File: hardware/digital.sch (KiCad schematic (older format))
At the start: 39 parts, among them U10 74LVC4245, U11 74LVC4245, U12 74LVC4245, U9 STM32F103V8Tx

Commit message: Schematic mainly done. Working on PCB layout in isolated blocks.
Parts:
- removed C49, C50, C51, C52, C53, C54, C55, C56, C57: 100n, Capacitor_SMD:C_0603_1608Metric, symbol Device:C
- removed U10, U11, U12: 74LVC4245, Package_SO:TSSOP-24_4.4x7.8mm_P0.65mm, symbol Logic_LevelTranslator:SN74AVC8T245PW
- added C17: 1u0, Capacitor_SMD:C_0603_1608Metric, symbol Device:C_Small
- added C18, C19: C_Small, Capacitor_SMD:C_0603_1608Metric, symbol Device:C_Small
- added C20: 10n, Capacitor_SMD:C_0603_1608Metric, symbol Device:C_Small
- added C28, C29, C30, C31, C32, C33, C34, C35, C36: 100n, Capacitor_SMD:C_0603_1608Metric, symbol Device:C
- added J10: Conn_02x03_Counter_Clockwise, Connector_PinSocket_2.54mm:PinSocket_2x03_P2.54mm_Vertical_SMD, symbol Connector_Generic:Conn_02x03_Counter_Clockwise
- added J11: Conn_02x05_Odd_Even, Connector_PinHeader_1.27mm:PinHeader_2x05_P1.27mm_Vertical_SMD, symbol Connector_Generic:Conn_02x05_Odd_Even
- added R10, R11, R9: 10K, Resistor_SMD:R_0603_1608Metric, symbol Device:R_Small
- added RN18, RN19, RN20, RN21, RN22, RN23: 4K7, Resistor_SMD:R_Array_Convex_4x0603, symbol Device:R_Pack04
- added SW1: SW_Push, symbol Switch:SW_Push
- added U10, U11, U9: 74LVC4245, Package_SO:TSSOP-24_4.4x7.8mm_P0.65mm, symbol Console2JAMMA:74LVC4245
- added Y1: 8MHz, Crystal:Crystal_SMD_5032-2Pin_5.0x3.2mm, symbol Device:Crystal_Small
- C16: renamed from C41; footprint Capacitor_SMD:C_0603_1608Metric -> Capacitor_SMD:C_0805_2012Metric
- C27: renamed from C48; footprint Capacitor_SMD:C_0603_1608Metric -> Capacitor_SMD:C_0805_2012Metric
- renumbered C42 to C21, C43 to C22, C44 to C23, C45 to C24, C46 to C25, C47 to C26, R14 to R12, R15 to R13, R16 to R14, U9 to U8
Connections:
- net labels added: Audio_Select_L, Audio_Select_Mono, Audio_Select_R, BOOT0, BOOT1, TCK_SWCLK, TDI_NC, TDO_TRACESWO, TMS_SWDIO, USB_D+, USB_D-, VOL_CLK, VOL_DATA_IN, VOL_LOAD_SHIFT, Video_Select_Blue, Video_Select_CSYNC, Video_Select_Green, Video_Select_Red, ~TRST~
- net labels removed: P1P2_Shifter_DIR
- wire segments 304 -> 453
- no-connect marks 1 -> 12
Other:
- note added: "Boot Loader Config"
- note added: "Cortex Debug Header"
- note added: "KEY"
- note added: "Non 5V tolerant I/O: PC0-5, PA1-7, PB0-1, 5"
- note removed: "3V3 I/O to and from Level Shifter"
- note removed: "Player 1"
- note removed: "Player 2"
- moved on the sheet: C16, C21, C22, C23, C24, C25, C26, C27, R12, R13, R14, RN10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

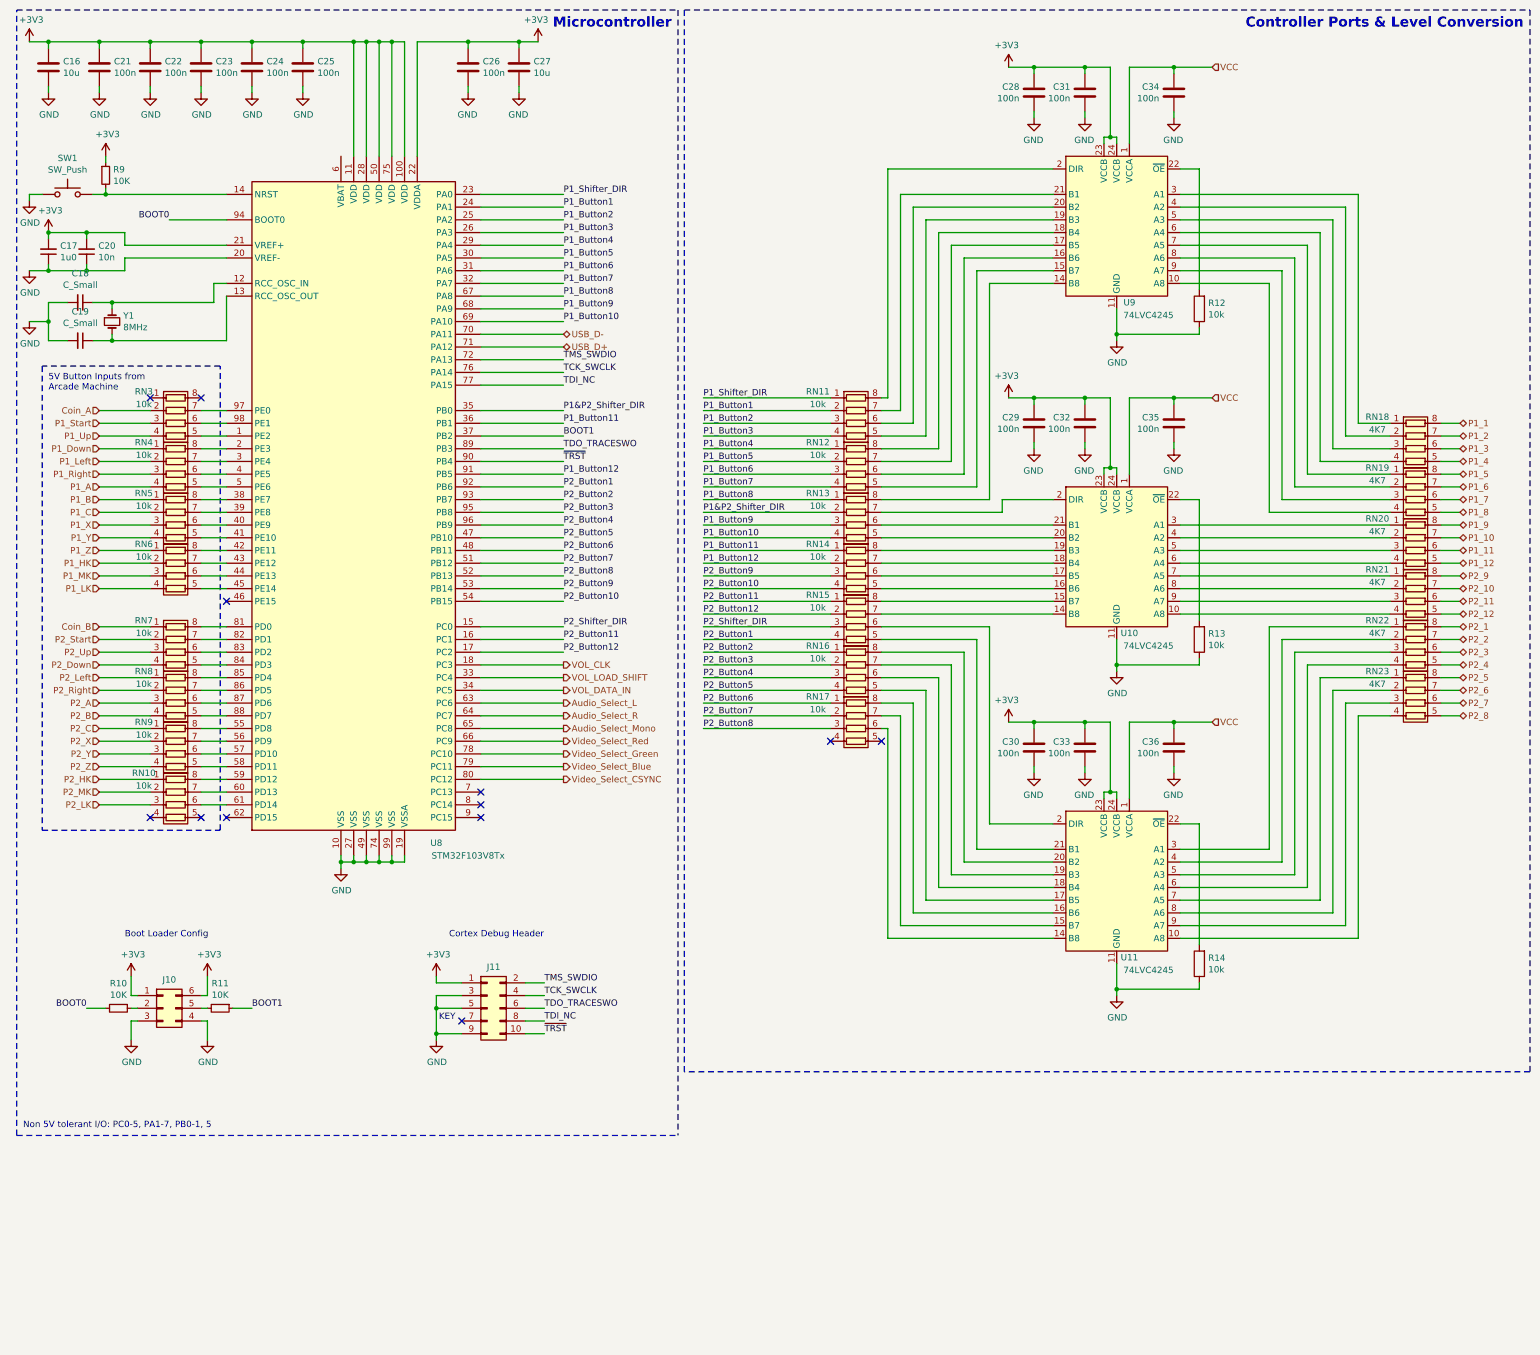
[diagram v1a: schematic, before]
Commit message: Completing the functionality of PCB layout. Require silkscreen placement still, though.
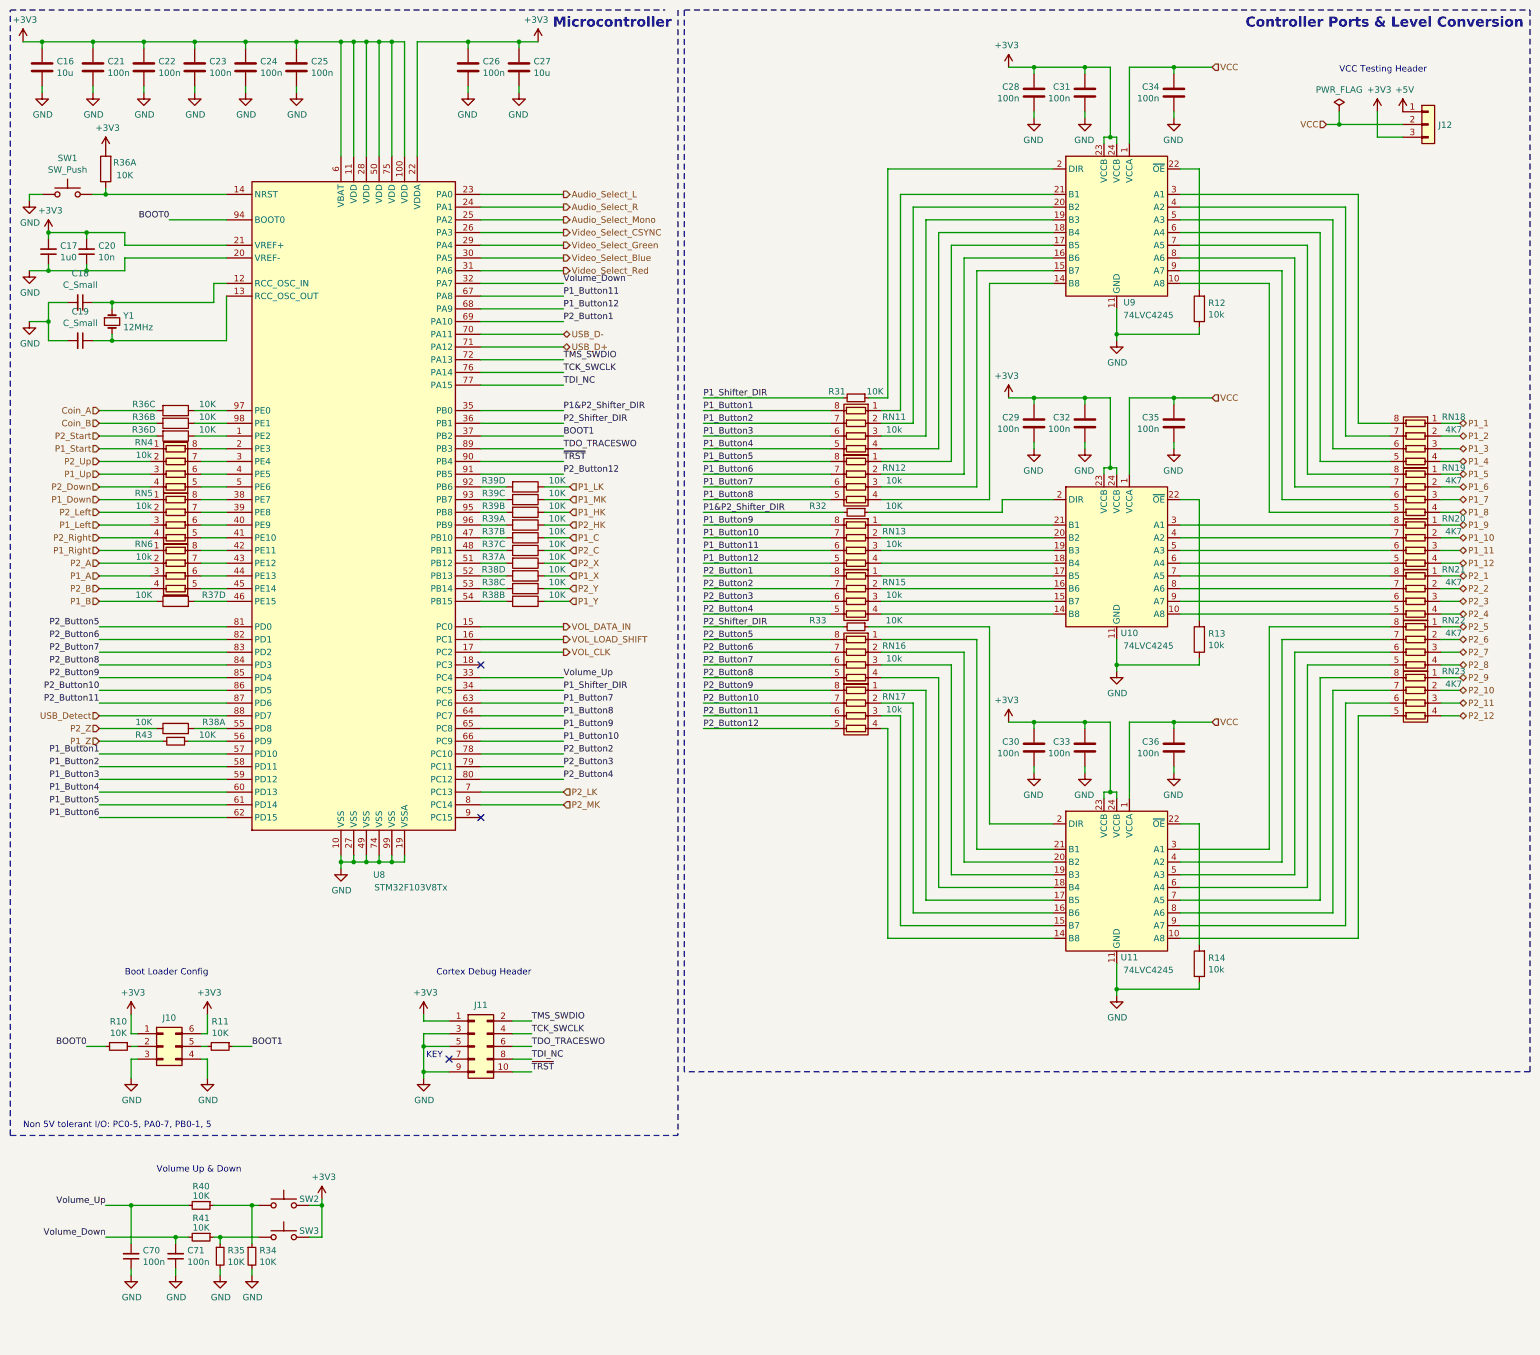
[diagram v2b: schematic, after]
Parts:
- removed R9: 10K, Resistor_SMD:R_0603_1608Metric, symbol Device:R_Small
- removed RN10, RN14, RN3, RN7, RN8, RN9: 10k, Resistor_SMD:R_Array_Convex_4x0603, symbol Device:R_Pack04
- added C70, C71: 100n, Capacitor_SMD:C_0603_1608Metric, symbol Device:C_Small
- added J12: Conn_01x03, Connector_PinHeader_2.54mm:PinHeader_1x03_P2.54mm_Vertical, symbol Connector_Generic:Conn_01x03
- added R31, R32, R33, R34, R35, R40, R41, R43: 10K, Resistor_SMD:R_0603_1608Metric, symbol Device:R_Small
- added R36, R37, R38, R39: 10K, Resistor_SMD:R_Array_Convex_4x0603, symbol Device:R_Pack04_Split
- added SW2, SW3: SW_Push, Console2JAMMA:SW_Push_SPST_NO_Alps_SKRP, symbol Switch:SW_Push
- SW1: footprint (none) -> Console2JAMMA:SW_Push_SPST_NO_Alps_SKRP
- Y1: value 8MHz -> 12MHz
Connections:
- net +3V3: now also U8.6 (VBAT), J12.3 (Pin_3), R36.1, SW2.2, SW3.2
- net Audio_Select_L: now also U8.23 (PA0); no longer U8.63 (PC6)
- net Audio_Select_Mono: now also U8.25 (PA2); no longer U8.65 (PC8)
- net Audio_Select_R: now also U8.24 (PA1); no longer U8.64 (PC7)
- net Coin_A: now also R36.3
- net Coin_B: now also R36.2
- net GND: now also C70.1, C71.1, R34.2, R35.2
- net P1&P2_Shifter_DIR: now also R32.2; no longer RN13.2 (R2.1)
- net P1_1: now also RN18.1 (R1.1); no longer RN18.8 (R1.2)
- net P1_10: now also RN20.2 (R2.1); no longer RN20.7 (R2.2)
- net P1_11: now also RN20.3 (R3.1); no longer RN20.6 (R3.2)
- net P1_12: now also RN20.4 (R4.1); no longer RN20.5 (R4.2)
- net P1_2: now also RN18.2 (R2.1); no longer RN18.7 (R2.2)
- net P1_3: now also RN18.3 (R3.1); no longer RN18.6 (R3.2)
- net P1_4: now also RN18.4 (R4.1); no longer RN18.5 (R4.2)
- net P1_5: now also RN19.1 (R1.1); no longer RN19.8 (R1.2)
- net P1_6: now also RN19.2 (R2.1); no longer RN19.7 (R2.2)
- net P1_7: now also RN19.3 (R3.1); no longer RN19.6 (R3.2)
- net P1_8: now also RN19.4 (R4.1); no longer RN19.5 (R4.2)
- net P1_9: now also RN20.1 (R1.1); no longer RN20.8 (R1.2)
- net P1_A: now also RN6.3 (R3.1); no longer RN4.4 (R4.1)
- net P1_B: now also R37.5; no longer RN5.1 (R1.1)
- net P1_Button1: now also RN11.8 (R1.2), U8.57 (PD10); no longer RN11.2 (R2.1), U8.24 (PA1)
- net P1_Button10: now also RN13.7 (R2.2), U8.66 (PC9); no longer RN13.4 (R4.1), U8.69 (PA10)
- net P1_Button11: now also RN13.6 (R3.2), U8.67 (PA8); no longer U8.36 (PB1)
- net P1_Button12: now also RN13.5 (R4.2), U8.68 (PA9); no longer U8.91 (PB5)
- net P1_Button2: now also RN11.7 (R2.2), U8.58 (PD11); no longer RN11.3 (R3.1), U8.25 (PA2)
- net P1_Button3: now also RN11.6 (R3.2), U8.59 (PD12); no longer RN11.4 (R4.1), U8.26 (PA3)
- net P1_Button4: now also RN11.5 (R4.2), U8.60 (PD13); no longer RN12.1 (R1.1), U8.29 (PA4)
- net P1_Button5: now also RN12.8 (R1.2), U8.61 (PD14); no longer RN12.2 (R2.1), U8.30 (PA5)
- net P1_Button6: now also RN12.7 (R2.2), U8.62 (PD15); no longer RN12.3 (R3.1), U8.31 (PA6)
- net P1_Button7: now also RN12.6 (R3.2), U8.63 (PC6); no longer RN12.4 (R4.1), U8.32 (PA7)
- net P1_Button8: now also RN12.5 (R4.2), U8.64 (PC7); no longer RN13.1 (R1.1), U8.67 (PA8)
- net P1_Button9: now also RN13.8 (R1.2), U8.65 (PC8); no longer RN13.3 (R3.1), U8.68 (PA9)
- net P1_C: now also R37.7; no longer RN5.2 (R2.1)
- net P1_Down: now also RN5.1 (R1.1); no longer RN4.1 (R1.1)
- net P1_HK: now also R39.7; no longer RN6.2 (R2.1)
- net P1_LK: now also R39.5; no longer RN6.4 (R4.1)
- net P1_Left: now also RN5.3 (R3.1); no longer RN4.2 (R2.1)
- net P1_MK: now also R39.6; no longer RN6.3 (R3.1)
- net P1_Right: now also RN6.1 (R1.1); no longer RN4.3 (R3.1)
- net P1_Shifter_DIR: now also U8.34 (PC5), R31.2; no longer RN11.1 (R1.1), U8.23 (PA0)
- net P1_Start: now also RN4.1 (R1.1)
- net P1_Up: now also RN4.3 (R3.1)
- net P1_X: now also R38.5; no longer RN5.3 (R3.1)
- net P1_Y: now also R38.7; no longer RN5.4 (R4.1)
- net P1_Z: now also R43.2; no longer RN6.1 (R1.1)
- net P2_1: now also RN21.1 (R1.1); no longer RN22.8 (R1.2)
- net P2_10: now also RN23.2 (R2.1); no longer RN21.7 (R2.2)
- net P2_11: now also RN23.3 (R3.1); no longer RN21.6 (R3.2)
- net P2_12: now also RN23.4 (R4.1); no longer RN21.5 (R4.2)
- net P2_2: now also RN21.2 (R2.1); no longer RN22.7 (R2.2)
- net P2_3: now also RN21.3 (R3.1); no longer RN22.6 (R3.2)
- net P2_4: now also RN21.4 (R4.1); no longer RN22.5 (R4.2)
- net P2_5: now also RN22.1 (R1.1); no longer RN23.8 (R1.2)
- net P2_6: now also RN22.2 (R2.1); no longer RN23.7 (R2.2)
- net P2_7: now also RN22.3 (R3.1); no longer RN23.6 (R3.2)
- net P2_8: now also RN22.4 (R4.1); no longer RN23.5 (R4.2)
- net P2_9: now also RN23.1 (R1.1); no longer RN21.8 (R1.2)
- net P2_A: now also RN6.2 (R2.1)
- net P2_B: now also RN6.4 (R4.1)
- net P2_Button1: now also RN15.8 (R1.2), U8.69 (PA10); no longer RN15.4 (R4.1), U8.92 (PB6)
- net P2_Button10: now also RN17.7 (R2.2), U8.86 (PD5); no longer U8.54 (PB15)
- net P2_Button11: now also RN17.6 (R3.2), U8.87 (PD6); no longer RN15.1 (R1.1), U8.16 (PC1)
- net P2_Button12: now also RN17.5 (R4.2), U8.91 (PB5); no longer RN15.2 (R2.1), U8.17 (PC2)
- net P2_Button2: now also RN15.7 (R2.2), U8.78 (PC10); no longer RN16.1 (R1.1), U8.93 (PB7)
- net P2_Button3: now also RN15.6 (R3.2), U8.79 (PC11); no longer RN16.2 (R2.1), U8.95 (PB8)
- net P2_Button4: now also RN15.5 (R4.2), U8.80 (PC12); no longer RN16.3 (R3.1), U8.96 (PB9)
- net P2_Button5: now also RN16.8 (R1.2), U8.81 (PD0); no longer RN16.4 (R4.1), U8.47 (PB10)
- net P2_Button6: now also RN16.7 (R2.2), U8.82 (PD1); no longer RN17.1 (R1.1), U8.48 (PB11)
- net P2_Button7: now also RN16.6 (R3.2), U8.83 (PD2); no longer RN17.2 (R2.1), U8.51 (PB12)
- net P2_Button8: now also RN16.5 (R4.2), U8.84 (PD3); no longer RN17.3 (R3.1), U8.52 (PB13)
- net P2_Button9: now also RN17.8 (R1.2), U8.85 (PD4); no longer U8.53 (PB14)
- net P2_C: now also R37.6
- net P2_Down: now also RN4.4 (R4.1)
- net P2_HK: now also R39.8
- net P2_LK: now also U8.7 (PC13)
- net P2_Left: now also RN5.2 (R2.1)
- net P2_MK: now also U8.8 (PC14)
- net P2_Right: now also RN5.4 (R4.1)
- net P2_Shifter_DIR: now also U8.36 (PB1), R33.2; no longer RN15.3 (R3.1), U8.15 (PC0)
- net P2_Start: now also R36.4
- net P2_Up: now also RN4.2 (R2.1)
- net P2_X: now also R37.8
- net P2_Y: now also R38.6
- net P2_Z: now also R38.8
- net VCC: now also J12.2 (Pin_2)
- net VOL_CLK: now also U8.17 (PC2); no longer U8.18 (PC3)
- net VOL_DATA_IN: now also U8.15 (PC0); no longer U8.34 (PC5)
- net VOL_LOAD_SHIFT: now also U8.16 (PC1); no longer U8.33 (PC4)
- net Video_Select_Blue: now also U8.30 (PA5); no longer U8.79 (PC11)
- net Video_Select_CSYNC: now also U8.26 (PA3); no longer U8.80 (PC12)
- net Video_Select_Green: now also U8.29 (PA4); no longer U8.78 (PC10)
- net Video_Select_Red: now also U8.31 (PA6); no longer U8.66 (PC9)
- net at U8.1 (PE2): now also R36.5
- net at U8.98 (PE1): now also R36.7
- net at U8.97 (PE0): now also R36.6
- net at U8.56 (PD9): now also R43.1
- net at U8.55 (PD8): now also R38.1
- net USB_Detect: now reaches U8.88 (PD7)
- net at SW1.2, U8.14 (NRST): now also R36.8
- net at U8.46 (PE15): now also R37.4
- net at U10.20 (B2): now also RN13.2 (R2.1); no longer RN13.5 (R4.2)
- net at U10.21 (B1): now also RN13.1 (R1.1); no longer RN13.6 (R3.2)
- net at U10.2 (DIR): now also R32.1; no longer RN13.7 (R2.2)
- net at U9.14 (B8): now also RN12.4 (R4.1); no longer RN13.8 (R1.2)
- net at U9.15 (B7): now also RN12.3 (R3.1); no longer RN12.5 (R4.2)
- net at U9.16 (B6): now also RN12.2 (R2.1); no longer RN12.6 (R3.2)
- net at U9.17 (B5): now also RN12.1 (R1.1); no longer RN12.7 (R2.2)
- net at U9.18 (B4): now also RN11.4 (R4.1); no longer RN12.8 (R1.2)
- net at U9.19 (B3): now also RN11.3 (R3.1); no longer RN11.5 (R4.2)
- net at U9.20 (B2): now also RN11.2 (R2.1); no longer RN11.6 (R3.2)
- net at U9.21 (B1): now also RN11.1 (R1.1); no longer RN11.7 (R2.2)
- net at U9.2 (DIR): now also R31.1; no longer RN11.8 (R1.2)
- net at U10.16 (B6): now also RN15.2 (R2.1)
- net at U10.17 (B5): now also RN15.1 (R1.1)
- net at U10.18 (B4): now also RN13.4 (R4.1)
- net at U10.19 (B3): now also RN13.3 (R3.1)
- net at RN17.4 (R4.1): now also U11.14 (B8)
- net at U11.15 (B7): now also RN17.3 (R3.1); no longer RN17.7 (R2.2)
- net at U11.16 (B6): now also RN17.2 (R2.1); no longer RN17.8 (R1.2)
- net at U11.17 (B5): now also RN17.1 (R1.1); no longer RN16.5 (R4.2)
- net at U11.18 (B4): now also RN16.4 (R4.1); no longer RN16.6 (R3.2)
- net at U11.19 (B3): now also RN16.3 (R3.1); no longer RN16.7 (R2.2)
- net at U11.20 (B2): now also RN16.2 (R2.1); no longer RN16.8 (R1.2)
- net at U11.21 (B1): now also RN16.1 (R1.1); no longer RN15.5 (R4.2)
- net at U11.2 (DIR): now also R33.1; no longer RN15.6 (R3.2)
- net at U10.14 (B8): now also RN15.4 (R4.1); no longer RN15.7 (R2.2)
- net at U10.15 (B7): now also RN15.3 (R3.1); no longer RN15.8 (R1.2)
- net at U9.10 (A8): now also RN19.5 (R4.2); no longer RN19.4 (R4.1)
- net at U9.3 (A1): now also RN18.8 (R1.2); no longer RN18.1 (R1.1)
- net at U9.4 (A2): now also RN18.7 (R2.2); no longer RN18.2 (R2.1)
- net at U9.5 (A3): now also RN18.6 (R3.2); no longer RN18.3 (R3.1)
- net at U9.6 (A4): now also RN18.5 (R4.2); no longer RN18.4 (R4.1)
- net at U9.7 (A5): now also RN19.8 (R1.2); no longer RN19.1 (R1.1)
- net at U9.8 (A6): now also RN19.7 (R2.2); no longer RN19.2 (R2.1)
- net at U9.9 (A7): now also RN19.6 (R3.2); no longer RN19.3 (R3.1)
- net at U10.10 (A8): now also RN21.5 (R4.2); no longer RN21.4 (R4.1)
- net at U10.3 (A1): now also RN20.8 (R1.2); no longer RN20.1 (R1.1)
- net at U10.4 (A2): now also RN20.7 (R2.2); no longer RN20.2 (R2.1)
- net at U10.5 (A3): now also RN20.6 (R3.2); no longer RN20.3 (R3.1)
- net at U10.6 (A4): now also RN20.5 (R4.2); no longer RN20.4 (R4.1)
- net at U10.7 (A5): now also RN21.8 (R1.2); no longer RN21.1 (R1.1)
- net at U10.8 (A6): now also RN21.7 (R2.2); no longer RN21.2 (R2.1)
- net at U10.9 (A7): now also RN21.6 (R3.2); no longer RN21.3 (R3.1)
- net at U11.10 (A8): now also RN23.5 (R4.2); no longer RN23.4 (R4.1)
- net at U11.3 (A1): now also RN22.8 (R1.2); no longer RN22.1 (R1.1)
- net at U11.4 (A2): now also RN22.7 (R2.2); no longer RN22.2 (R2.1)
- net at U11.5 (A3): now also RN22.6 (R3.2); no longer RN22.3 (R3.1)
- net at U11.6 (A4): now also RN22.5 (R4.2); no longer RN22.4 (R4.1)
- net at U11.7 (A5): now also RN23.8 (R1.2); no longer RN23.1 (R1.1)
- net at U11.8 (A6): now also RN23.7 (R2.2); no longer RN23.2 (R2.1)
- net at U11.9 (A7): now also RN23.6 (R3.2); no longer RN23.3 (R3.1)
- new net: R37.2, U8.47 (PB10)
- new net: R37.3, U8.48 (PB11)
- new net: R37.1, U8.51 (PB12)
- new net: R38.4, U8.52 (PB13)
- new net: R38.3, U8.53 (PB14)
- new net: R38.2, U8.54 (PB15)
- new net: R39.4, U8.92 (PB6)
- new net: R39.3, U8.93 (PB7)
- new net: R39.2, U8.95 (PB8)
- new net: R39.1, U8.96 (PB9)
- new net: R34.1, R40.1, SW2.1
- new net: R35.1, R41.1, SW3.1
- new net +5V: J12.1 (Pin_1)
- new net Volume_Down: C71.2, R41.2, U8.32 (PA7)
- new net Volume_Up: C70.2, R40.2, U8.33 (PC4)
- no-connect marks 12 -> 3
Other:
- note added: "Non 5V tolerant I/O: PC0-5, PA0-7, PB0-1, 5"
- note added: "VCC Testing Header"
- note added: "Volume Up & Down"
- note removed: "5V Button Inputs from \nArcade Machine"
- note removed: "Non 5V tolerant I/O: PC0-5, PA1-7, PB0-1, 5"
- moved on the sheet: C16, C21, C22, C23, C24, C25, J10, J11, R10, R11, RN15, RN16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

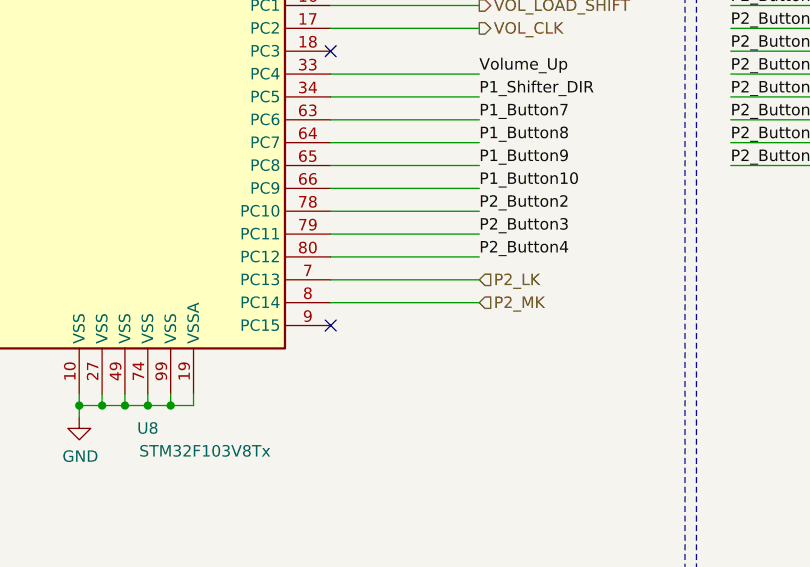
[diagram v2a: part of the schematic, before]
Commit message: Updating silkscreen placement and fixing up a few issues with layout. Still require via stitching to be done. Adding CERN OHL S license in hardware folder.
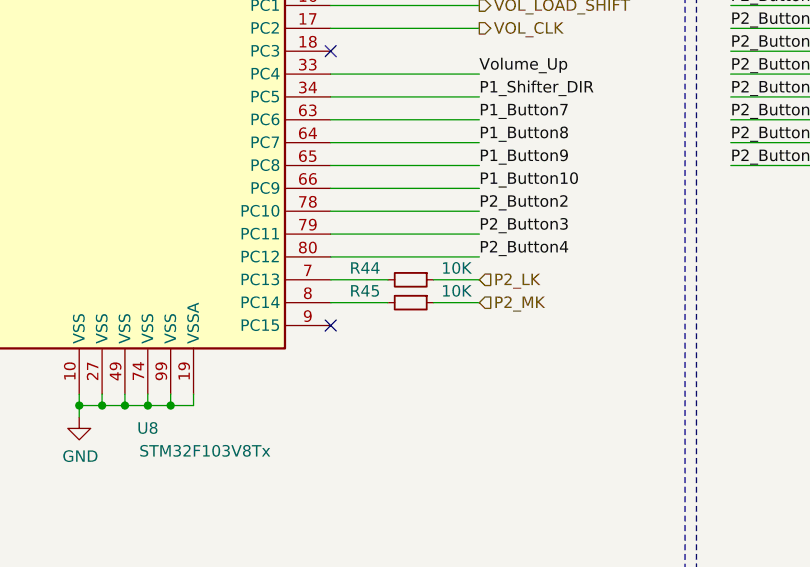
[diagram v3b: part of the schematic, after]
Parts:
- added R44, R45: 10K, Resistor_SMD:R_0603_1608Metric, symbol Device:R_Small
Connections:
- net P2_LK: now also R44.1; no longer U8.7 (PC13)
- net P2_MK: now also R45.1; no longer U8.8 (PC14)
- new net: R44.2, U8.7 (PC13)
- new net: R45.2, U8.8 (PC14)
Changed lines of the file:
@@
 Sheet 4 4
 Title "JAMMA2Console"
-Date "2020-04-06"
+Date "2020-04-20"
 Rev "1"
 Comp "Gold"
@@
 USB_Detect
 Wire Wire Line
-	4200 6700 4850 6700
+	4200 6700 4450 6700
 Wire Wire Line
 	5950 5400 7050 5400
@@
 Volume_Down
 Wire Wire Line
-	4200 6800 4850 6800
+	4200 6800 4450 6800
 NoConn ~ 4200 6900
 NoConn ~ 4200 5700
@@
 Wire Wire Line
 	3100 800  3200 800
+$Comp
+L Device:R_Small R44
+U 1 1 5EAE5830
+P 4550 6700
+F 0 "R44" V 4500 6500 50  0000 C CNN
+F 1 "10K" V 4500 6900 50  0000 C CNN
+F 2 "Resistor_SMD:R_0603_1608Metric" H 4550 6700 50  0001 C CNN
+F 3 "~" H 4550 6700 50  0001 C CNN
+	1    4550 6700
+	0    1    1    0
+$EndComp
+Wire Wire Line
+	4650 6700 4850 6700
+$Comp
+L Device:R_Small R45
+U 1 1 5EAE5E95
+P 4550 6800
+F 0 "R45" V 4500 6600 50  0000 C CNN
+F 1 "10K" V 4500 7000 50  0000 C CNN
+F 2 "Resistor_SMD:R_0603_1608Metric" H 4550 6800 50  0001 C CNN
+F 3 "~" H 4550 6800 50  0001 C CNN
+	1    4550 6800
+	0    1    1    0
+$EndComp
+Wire Wire Line
+	4650 6800 4850 6800
 $EndSCHEMATC
